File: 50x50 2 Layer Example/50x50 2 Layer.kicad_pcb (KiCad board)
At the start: 2 copper layers, 50 x 50 mm, 76 parts, among them J1 Conn_01x02, J2 Conn_01x02, J3 USB_C_Receptacle_USB2.0_14P, J4 Conn_01x03, J5 Conn_01x04, SW1 SW_SPST, SW2 Reset, U1 RP2040, U2 W25Q128JVPIQ TR, U3 Voltage Regulator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

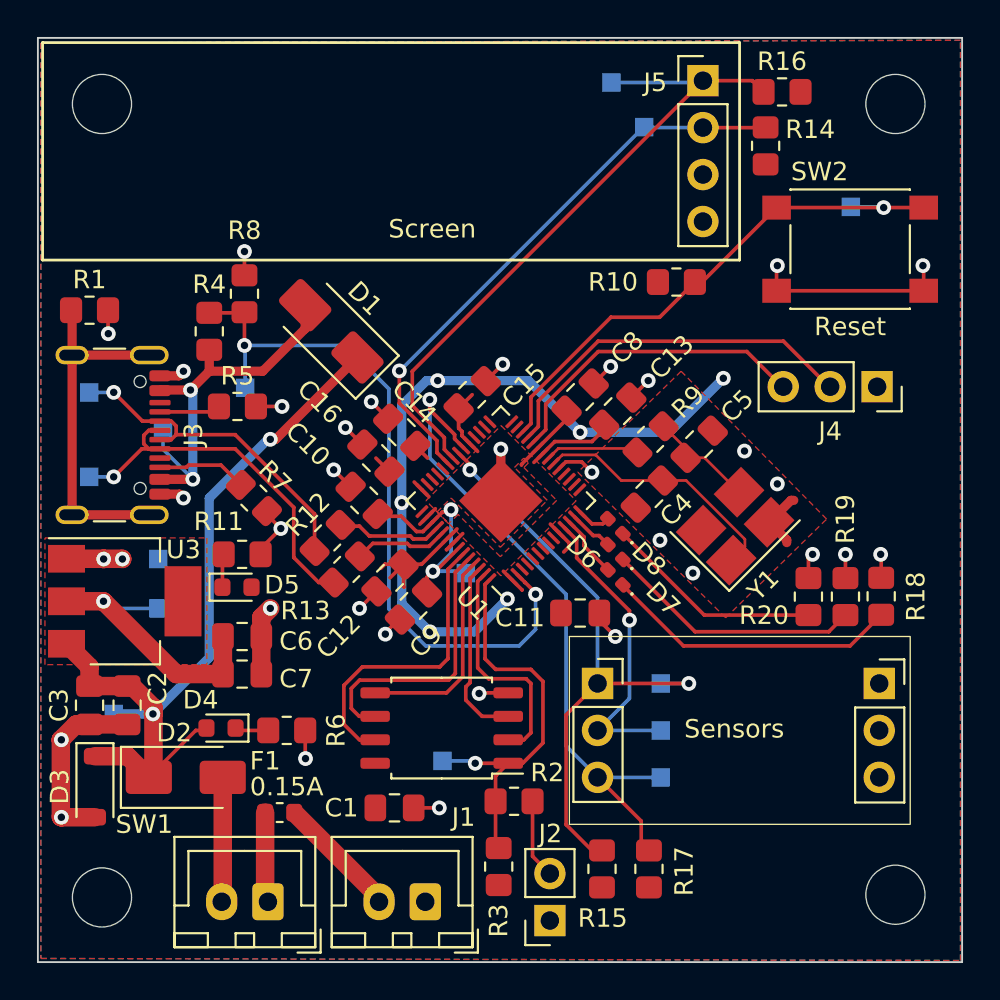
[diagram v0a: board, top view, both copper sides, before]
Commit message: Fixed screen connector and tidied GND plane
The OLED screen connector was flipped, so fixed that. Tidied up some long GND paths as well.
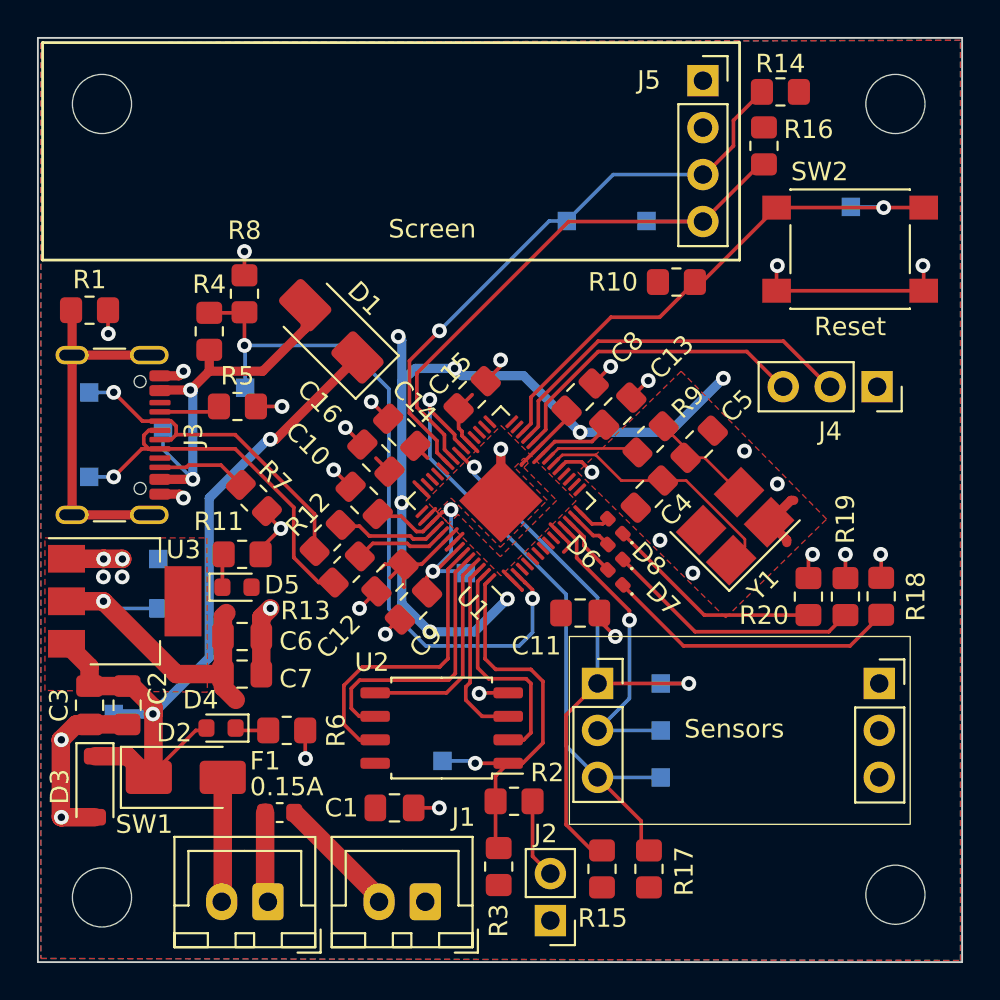
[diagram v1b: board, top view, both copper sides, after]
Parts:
- J2: footprint Connector_PinSocket_2.54mm:PinSocket_1x02_P2.54mm_Vertical -> Connector_PinHeader_2.54mm:PinHeader_1x02_P2.54mm_Vertical
- J5: footprint Connector_PinHeader_2.54mm:PinHeader_1x04_P2.54mm_Vertical -> Connector_PinSocket_2.54mm:PinSocket_1x04_P2.54mm_Vertical
- moved TP14 7.73 mm to (111.1, 47.2)
- moved TP12 6.59 mm to (106.8, 47.2)
- moved R16 3.08 mm to (117.5, 43.2), turned to 90 degrees
- moved R14 3.03 mm to (118.4, 40.3), turned to 0 degrees
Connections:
- J5 pad 1: I2C0_SDA -> GND
- J5 pad 2: I2C0_SCL -> +3V3
- J5 pad 3: +3V3 -> I2C0_SCL
- J5 pad 4: GND -> I2C0_SDA
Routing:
- net +3V3: track 78.2 -> 85.1 mm, vias 7 -> 8
- net I2C0_SDA: track 36.4 -> 31.9 mm
- net I2C0_SCL: track 31.4 -> 32.3 mm
- net GND: track 66.4 -> 66.6 mm, vias 34 -> 36
